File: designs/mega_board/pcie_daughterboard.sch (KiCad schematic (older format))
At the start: 13 parts

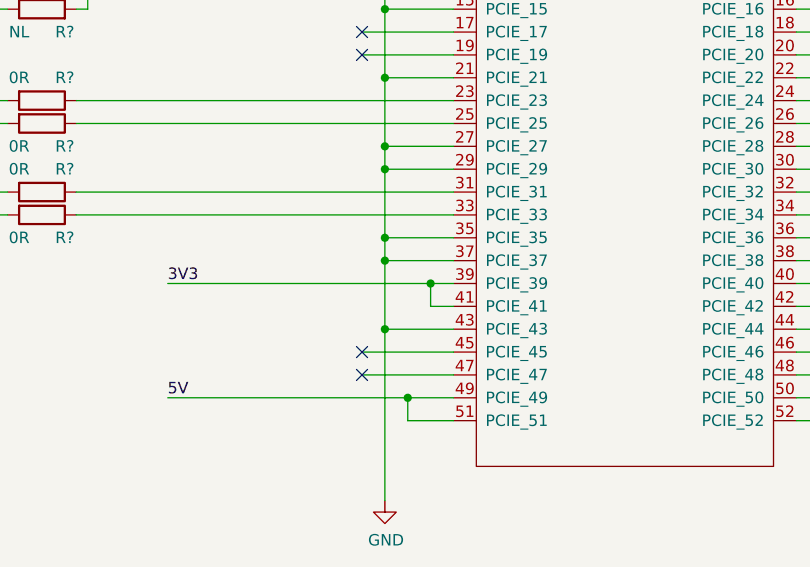
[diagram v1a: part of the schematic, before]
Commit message: Change PCIe pin 37 ground connection to not connected. Fixes #37
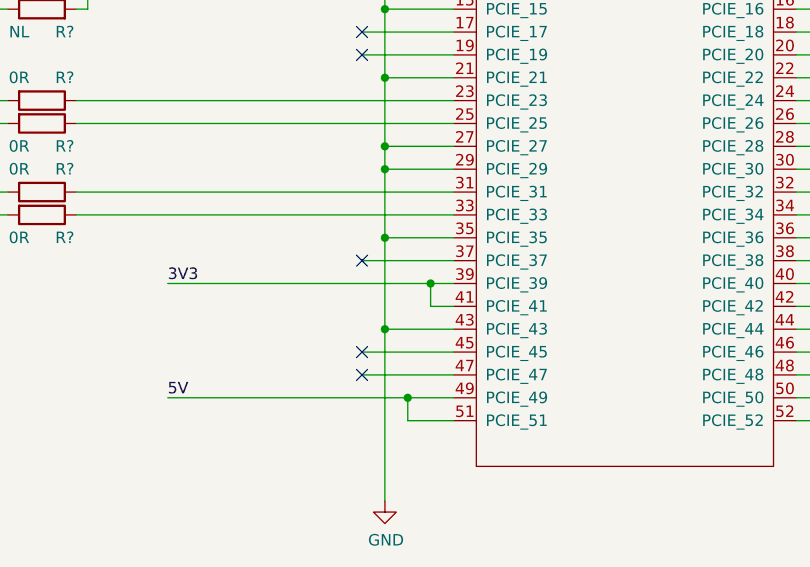
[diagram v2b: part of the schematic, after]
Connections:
- net GND: no longer U?.37 (PCIE_37)
- no-connect marks 13 -> 14
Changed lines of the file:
@@
 $Descr A4 11693 8268
 encoding utf-8
-Sheet 8 14
+Sheet 11 14
 Title "LibreRouter - Megaboard"
 Date "2019-06-26"
@@
 	4650 4400 4650 4700
 Connection ~ 4650 4700
-Wire Wire Line
-	4650 4700 4650 4800
 Connection ~ 4650 5100
 Wire Wire Line
@@
 Wire Wire Line
 	3000 4600 2500 4600
-Connection ~ 4650 4800
-Wire Wire Line
-	4650 4800 4650 5100
 NoConn ~ 4550 3800
 NoConn ~ 4550 3900
@@
 	4650 5100 4950 5100
 Wire Wire Line
-	4650 4800 4950 4800
-Wire Wire Line
 	4650 4700 4950 4700
 Wire Wire Line
@@
 Wire Wire Line
 	6450 5100 7400 5100
+Wire Wire Line
+	4650 4700 4650 5100
+NoConn ~ 4550 4800
+Wire Wire Line
+	4550 4800 4950 4800
 $EndSCHEMATC

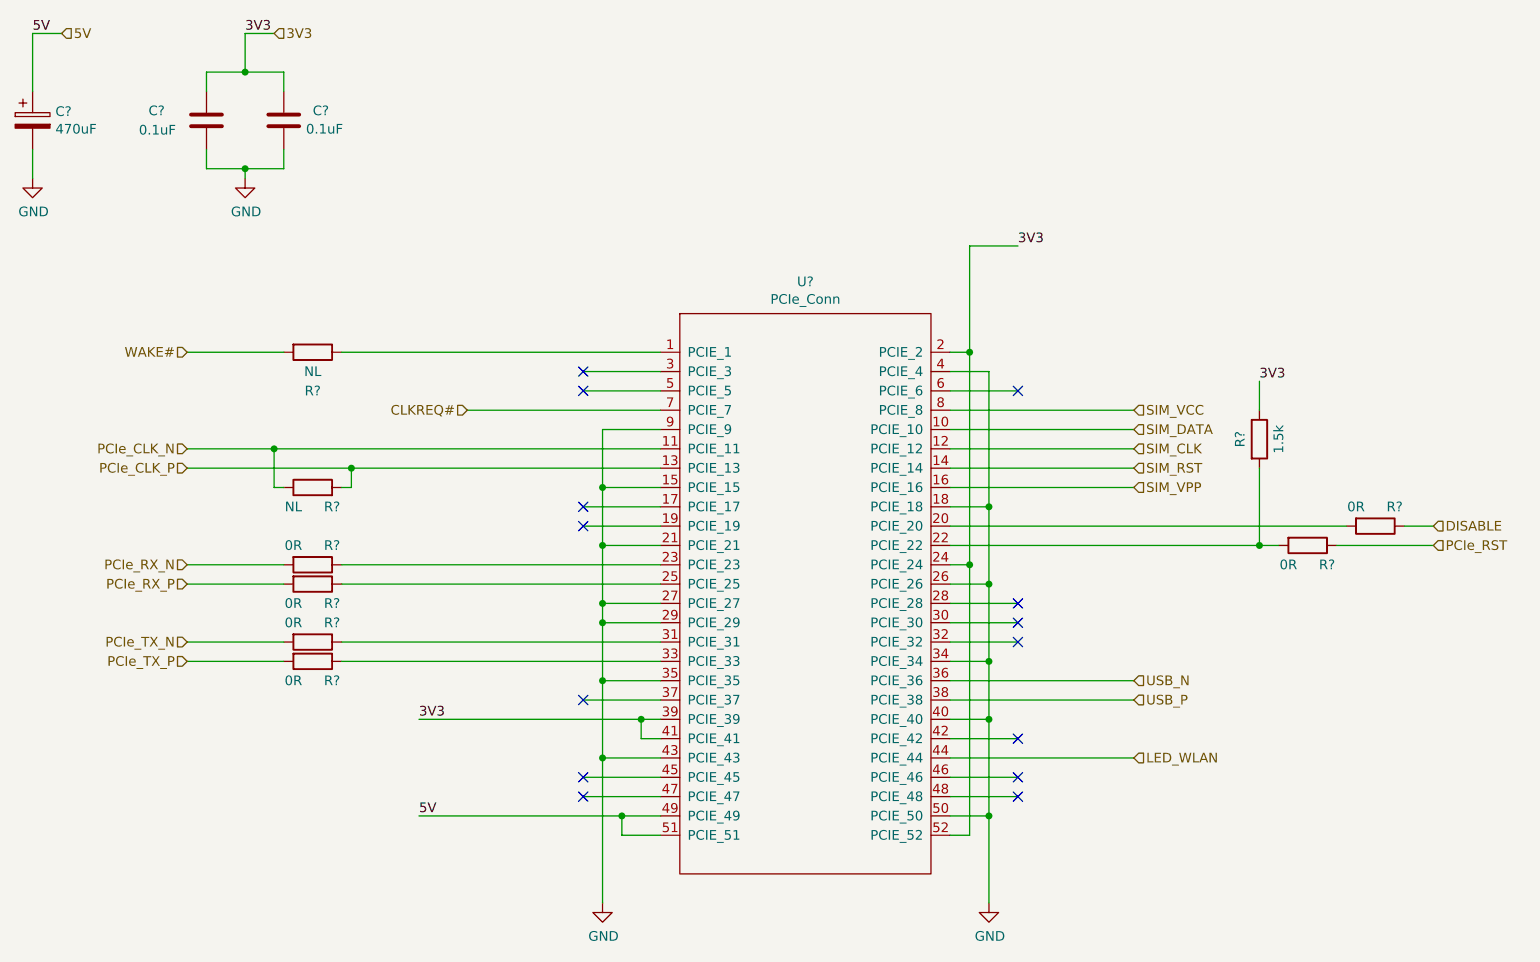
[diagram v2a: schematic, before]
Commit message: Enumerate components as is in eagle design.
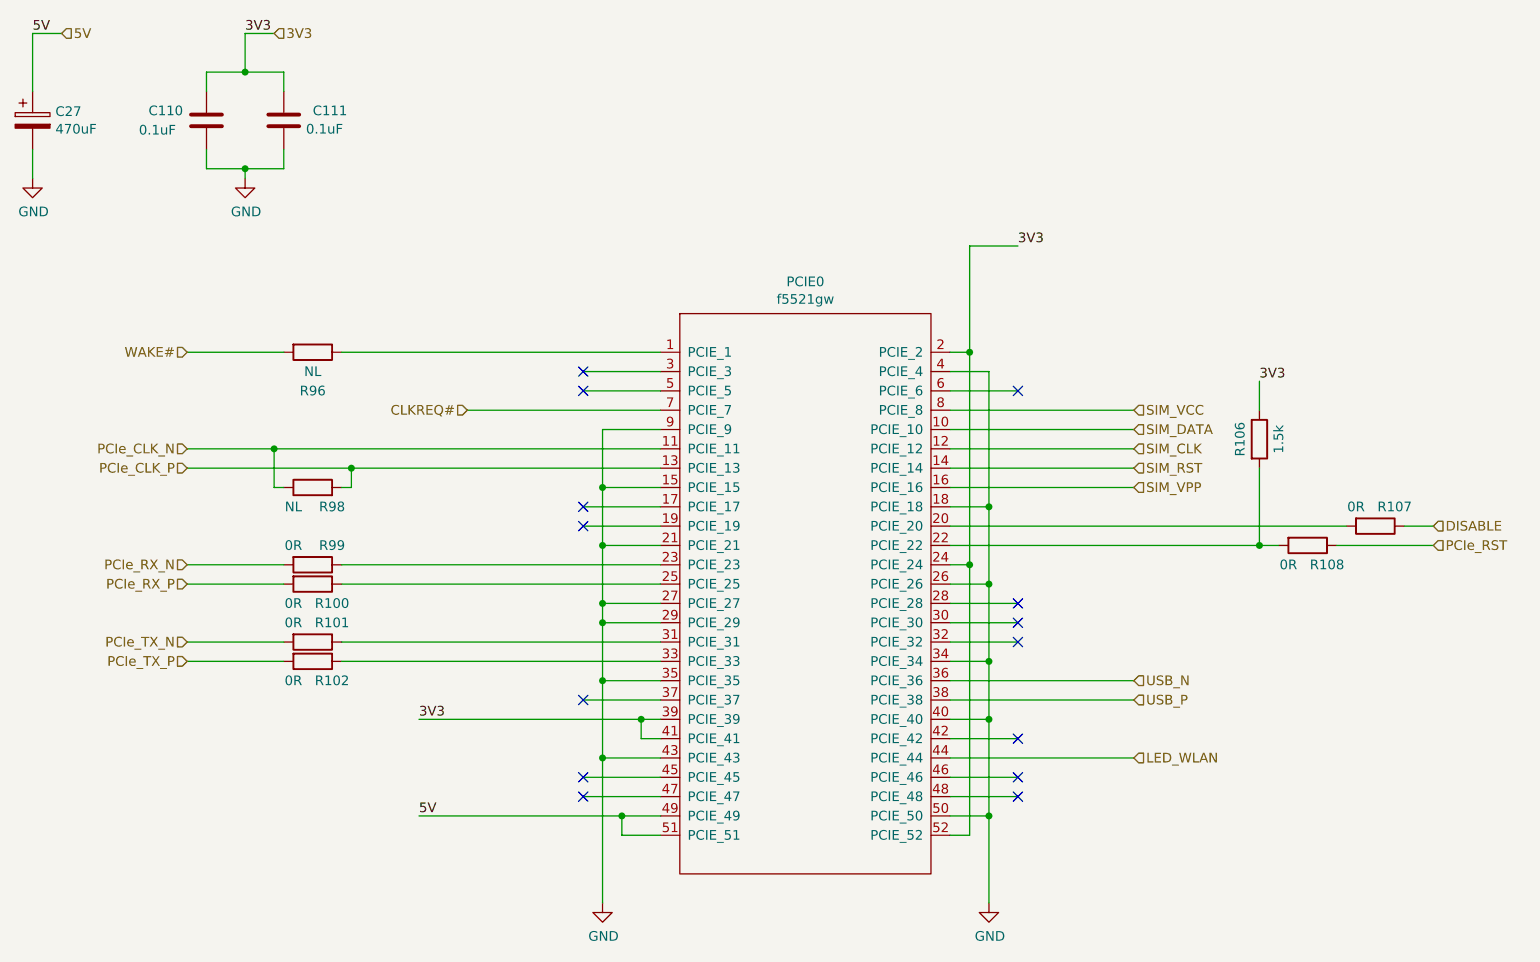
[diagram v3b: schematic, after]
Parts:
- C110, C111: renamed from C?; footprint (none) -> LibreRouter_MegaBoard:C0402
- C27: renamed from C?; footprint (none) -> LibreRouter_MegaBoard:UD-6,3X7,7_NICHICON
- PCIE0: renamed from U?; value PCIe_Conn -> f5521gw; footprint (none) -> LibreRouter_MegaBoard:MINI-PCI-E-FULL
- R100, R101, R102, R106, R107, R108, R96, R98, R99: renamed from R?; footprint (none) -> LibreRouter_MegaBoard:R0402
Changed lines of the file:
@@
 SIM_DATA
 $Comp
-L PCIe_Conn:PCIe_Conn U?
+L PCIe_Conn:PCIe_Conn PCIE0
 U 1 1 5D19C7E9
 P 5700 4250
-AR Path="/5D032C97/5D19C7E9" Ref="U?"  Part="1"
-AR Path="/5D1650F5/5D19C7E9" Ref="U?"  Part="1"
+AR Path="/5D032C97/5D19C7E9" Ref="PCIE0"  Part="1"
+AR Path="/5D1650F5/5D19C7E9" Ref="PCIE1"  Part="1"
 AR Path="/5D19C7E9" Ref="U?"  Part="1"
-F 0 "U?" H 5700 5865 50  0000 C CNN
-F 1 "PCIe_Conn" H 5700 5774 50  0000 C CNN
-F 2 "" H 5700 4250 50  0001 C CNN
+F 0 "PCIE0" H 5700 5865 50  0000 C CNN
+F 1 "f5521gw" H 5700 5774 50  0000 C CNN
+F 2 "LibreRouter_MegaBoard:MINI-PCI-E-FULL" H 5700 4250 50  0001 C CNN
 F 3 "" H 5700 4250 50  0001 C CNN
 	1    5700 4250
@@
 NoConn ~ 6800 5300
 $Comp
-L power:GND #PWR?
+L power:GND #PWR0173
 U 1 1 5D19F8AF
 P 6650 5850
-AR Path="/5D032C97/5D19F8AF" Ref="#PWR?"  Part="1"
-AR Path="/5D1650F5/5D19F8AF" Ref="#PWR?"  Part="1"
-F 0 "#PWR?" H 6650 5600 50  0001 C CNN
+AR Path="/5D032C97/5D19F8AF" Ref="#PWR0173"  Part="1"
+AR Path="/5D1650F5/5D19F8AF" Ref="#PWR0190"  Part="1"
+F 0 "#PWR0190" H 6650 5600 50  0001 C CNN
 F 1 "GND" H 6655 5677 50  0000 C CNN
 F 2 "" H 6650 5850 50  0001 C CNN
@@
 	6550 4100 6550 3000
 $Comp
-L Device:R R?
+L Device:R R108
 U 1 1 5D1A0459
 P 8300 4000
-AR Path="/5D032C97/5D1A0459" Ref="R?"  Part="1"
-AR Path="/5D1650F5/5D1A0459" Ref="R?"  Part="1"
-F 0 "R?" V 8400 4100 50  0000 C CNN
+AR Path="/5D032C97/5D1A0459" Ref="R108"  Part="1"
+AR Path="/5D1650F5/5D1A0459" Ref="R118"  Part="1"
+F 0 "R108" V 8400 4100 50  0000 C CNN
 F 1 "0R" V 8400 3900 50  0000 C CNN
-F 2 "" V 8230 4000 50  0001 C CNN
+F 2 "LibreRouter_MegaBoard:R0402" V 8230 4000 50  0001 C CNN
 F 3 "~" H 8300 4000 50  0001 C CNN
 	1    8300 4000
@@
 $EndComp
 $Comp
-L Device:R R?
+L Device:R R107
 U 1 1 5D1A04F3
 P 8650 3900
-AR Path="/5D032C97/5D1A04F3" Ref="R?"  Part="1"
-AR Path="/5D1650F5/5D1A04F3" Ref="R?"  Part="1"
-F 0 "R?" V 8550 4000 50  0000 C CNN
+AR Path="/5D032C97/5D1A04F3" Ref="R107"  Part="1"
+AR Path="/5D1650F5/5D1A04F3" Ref="R117"  Part="1"
+F 0 "R107" V 8550 4000 50  0000 C CNN
 F 1 "0R" V 8550 3800 50  0000 C CNN
-F 2 "" V 8580 3900 50  0001 C CNN
+F 2 "LibreRouter_MegaBoard:R0402" V 8580 3900 50  0001 C CNN
 F 3 "~" H 8650 3900 50  0001 C CNN
 	1    8650 3900
@@
 $EndComp
 $Comp
-L Device:R R?
+L Device:R R106
 U 1 1 5D1A051B
 P 8050 3450
-AR Path="/5D032C97/5D1A051B" Ref="R?"  Part="1"
-AR Path="/5D1650F5/5D1A051B" Ref="R?"  Part="1"
-F 0 "R?" V 7950 3450 50  0000 C CNN
+AR Path="/5D032C97/5D1A051B" Ref="R106"  Part="1"
+AR Path="/5D1650F5/5D1A051B" Ref="R116"  Part="1"
+F 0 "R106" V 7950 3450 50  0000 C CNN
 F 1 "1.5k" V 8150 3450 50  0000 C CNN
-F 2 "" V 7980 3450 50  0001 C CNN
+F 2 "LibreRouter_MegaBoard:R0402" V 7980 3450 50  0001 C CNN
 F 3 "~" H 8050 3450 50  0001 C CNN
 	1    8050 3450
@@
 	8800 3900 8950 3900
 $Comp
-L Device:R R?
+L Device:R R96
 U 1 1 5D1A5891
 P 3150 3000
-AR Path="/5D032C97/5D1A5891" Ref="R?"  Part="1"
-AR Path="/5D1650F5/5D1A5891" Ref="R?"  Part="1"
-F 0 "R?" V 3350 3000 50  0000 C CNN
+AR Path="/5D032C97/5D1A5891" Ref="R96"  Part="1"
+AR Path="/5D1650F5/5D1A5891" Ref="R20"  Part="1"
+F 0 "R96" V 3350 3000 50  0000 C CNN
 F 1 "NL" V 3250 3000 50  0000 C CNN
-F 2 "" V 3080 3000 50  0001 C CNN
+F 2 "LibreRouter_MegaBoard:R0402" V 3080 3000 50  0001 C CNN
 F 3 "~" H 3150 3000 50  0001 C CNN
 	1    3150 3000
@@
 	2500 3600 3350 3600
 $Comp
-L Device:R R?
+L Device:R R98
 U 1 1 5D1AF5AD
 P 3150 3700
-AR Path="/5D032C97/5D1AF5AD" Ref="R?"  Part="1"
-AR Path="/5D1650F5/5D1AF5AD" Ref="R?"  Part="1"
-F 0 "R?" V 3050 3600 50  0000 C CNN
+AR Path="/5D032C97/5D1AF5AD" Ref="R98"  Part="1"
+AR Path="/5D1650F5/5D1AF5AD" Ref="R49"  Part="1"
+F 0 "R98" V 3050 3600 50  0000 C CNN
 F 1 "NL" V 3050 3800 50  0000 C CNN
-F 2 "" V 3080 3700 50  0001 C CNN
+F 2 "LibreRouter_MegaBoard:R0402" V 3080 3700 50  0001 C CNN
 F 3 "~" H 3150 3700 50  0001 C CNN
 	1    3150 3700
@@
 3V3
 $Comp
-L Device:C C?
+L Device:C C110
 U 1 1 5D1C5785
 P 2600 1800
-AR Path="/5D032C97/5D1C5785" Ref="C?"  Part="1"
-AR Path="/5D1650F5/5D1C5785" Ref="C?"  Part="1"
-F 0 "C?" H 2300 1850 50  0000 L CNN
+AR Path="/5D032C97/5D1C5785" Ref="C110"  Part="1"
+AR Path="/5D1650F5/5D1C5785" Ref="C75"  Part="1"
+F 0 "C110" H 2300 1850 50  0000 L CNN
 F 1 "0.1uF" H 2250 1750 50  0000 L CNN
-F 2 "" H 2638 1650 50  0001 C CNN
+F 2 "LibreRouter_MegaBoard:C0402" H 2638 1650 50  0001 C CNN
 F 3 "~" H 2600 1800 50  0001 C CNN
 	1    2600 1800
@@
 $EndComp
 $Comp
-L Device:C C?
+L Device:C C111
 U 1 1 5D1C583F
 P 3000 1800
-AR Path="/5D032C97/5D1C583F" Ref="C?"  Part="1"
-AR Path="/5D1650F5/5D1C583F" Ref="C?"  Part="1"
-F 0 "C?" H 3150 1850 50  0000 L CNN
+AR Path="/5D032C97/5D1C583F" Ref="C111"  Part="1"
+AR Path="/5D1650F5/5D1C583F" Ref="C116"  Part="1"
+F 0 "C111" H 3150 1850 50  0000 L CNN
 F 1 "0.1uF" H 3115 1755 50  0000 L CNN
-F 2 "" H 3038 1650 50  0001 C CNN
+F 2 "LibreRouter_MegaBoard:C0402" H 3038 1650 50  0001 C CNN
 F 3 "~" H 3000 1800 50  0001 C CNN
 	1    3000 1800
@@
 $EndComp
 $Comp
-L power:GND #PWR?
+L power:GND #PWR0174
 U 1 1 5D1C58DE
 P 2800 2100
-AR Path="/5D032C97/5D1C58DE" Ref="#PWR?"  Part="1"
-AR Path="/5D1650F5/5D1C58DE" Ref="#PWR?"  Part="1"
-F 0 "#PWR?" H 2800 1850 50  0001 C CNN
+AR Path="/5D032C97/5D1C58DE" Ref="#PWR0174"  Part="1"
+AR Path="/5D1650F5/5D1C58DE" Ref="#PWR0191"  Part="1"
+F 0 "#PWR0191" H 2800 1850 50  0001 C CNN
 F 1 "GND" H 2805 1927 50  0000 C CNN
 F 2 "" H 2800 2100 50  0001 C CNN
@@
 	2950 1350 2800 1350
 $Comp
-L power:GND #PWR?
+L power:GND #PWR0175
 U 1 1 5D1D537C
 P 1700 2100
-AR Path="/5D032C97/5D1D537C" Ref="#PWR?"  Part="1"
-AR Path="/5D1650F5/5D1D537C" Ref="#PWR?"  Part="1"
-F 0 "#PWR?" H 1700 1850 50  0001 C CNN
+AR Path="/5D032C97/5D1D537C" Ref="#PWR0175"  Part="1"
+AR Path="/5D1650F5/5D1D537C" Ref="#PWR0192"  Part="1"
+F 0 "#PWR0192" H 1700 1850 50  0001 C CNN
 F 1 "GND" H 1705 1927 50  0000 C CNN
 F 2 "" H 1700 2100 50  0001 C CNN
@@
 	1850 1350 1700 1350
 $Comp
-L Device:CP C?
+L Device:CP C27
 U 1 1 5D1D8CB3
 P 1700 1800
-AR Path="/5D032C97/5D1D8CB3" Ref="C?"  Part="1"
-AR Path="/5D1650F5/5D1D8CB3" Ref="C?"  Part="1"
-F 0 "C?" H 1818 1846 50  0000 L CNN
+AR Path="/5D032C97/5D1D8CB3" Ref="C27"  Part="1"
+AR Path="/5D1650F5/5D1D8CB3" Ref="C43"  Part="1"
+F 0 "C27" H 1818 1846 50  0000 L CNN
 F 1 "470uF" H 1818 1755 50  0000 L CNN
-F 2 "" H 1738 1650 50  0001 C CNN
+F 2 "LibreRouter_MegaBoard:UD-6,3X7,7_NICHICON" H 1738 1650 50  0001 C CNN
 F 3 "~" H 1700 1800 50  0001 C CNN
 	1    1700 1800
@@
 	2500 4100 3000 4100
 $Comp
-L Device:R R?
+L Device:R R99
 U 1 1 5D1F3D95
 P 3150 4100
-AR Path="/5D032C97/5D1F3D95" Ref="R?"  Part="1"
-AR Path="/5D1650F5/5D1F3D95" Ref="R?"  Part="1"
-F 0 "R?" V 3050 4200 50  0000 C CNN
+AR Path="/5D032C97/5D1F3D95" Ref="R99"  Part="1"
+AR Path="/5D1650F5/5D1F3D95" Ref="R80"  Part="1"
+F 0 "R99" V 3050 4200 50  0000 C CNN
 F 1 "0R" V 3050 4000 50  0000 C CNN
-F 2 "" V 3080 4100 50  0001 C CNN
+F 2 "LibreRouter_MegaBoard:R0402" V 3080 4100 50  0001 C CNN
 F 3 "~" H 3150 4100 50  0001 C CNN
 	1    3150 4100
@@
 $EndComp
 $Comp
-L Device:R R?
+L Device:R R100
 U 1 1 5D1F3F5D
 P 3150 4200
-AR Path="/5D032C97/5D1F3F5D" Ref="R?"  Part="1"
-AR Path="/5D1650F5/5D1F3F5D" Ref="R?"  Part="1"
-F 0 "R?" V 3250 4300 50  0000 C CNN
+AR Path="/5D032C97/5D1F3F5D" Ref="R100"  Part="1"
+AR Path="/5D1650F5/5D1F3F5D" Ref="R110"  Part="1"
+F 0 "R100" V 3250 4300 50  0000 C CNN
 F 1 "0R" V 3250 4100 50  0000 C CNN
-F 2 "" V 3080 4200 50  0001 C CNN
+F 2 "LibreRouter_MegaBoard:R0402" V 3080 4200 50  0001 C CNN
 F 3 "~" H 3150 4200 50  0001 C CNN
 	1    3150 4200
@@
 	2500 4500 3000 4500
 $Comp
-L Device:R R?
+L Device:R R101
 U 1 1 5D1F7584
 P 3150 4500
-AR Path="/5D032C97/5D1F7584" Ref="R?"  Part="1"
-AR Path="/5D1650F5/5D1F7584" Ref="R?"  Part="1"
-F 0 "R?" V 3050 4600 50  0000 C CNN
+AR Path="/5D032C97/5D1F7584" Ref="R101"  Part="1"
+AR Path="/5D1650F5/5D1F7584" Ref="R111"  Part="1"
+F 0 "R101" V 3050 4600 50  0000 C CNN
 F 1 "0R" V 3050 4400 50  0000 C CNN
-F 2 "" V 3080 4500 50  0001 C CNN
+F 2 "LibreRouter_MegaBoard:R0402" V 3080 4500 50  0001 C CNN
 F 3 "~" H 3150 4500 50  0001 C CNN
 	1    3150 4500
@@
 $EndComp
 $Comp
-L Device:R R?
+L Device:R R102
 U 1 1 5D1F758C
 P 3150 4600
-AR Path="/5D032C97/5D1F758C" Ref="R?"  Part="1"
-AR Path="/5D1650F5/5D1F758C" Ref="R?"  Part="1"
-F 0 "R?" V 3250 4700 50  0000 C CNN
+AR Path="/5D032C97/5D1F758C" Ref="R102"  Part="1"
+AR Path="/5D1650F5/5D1F758C" Ref="R112"  Part="1"
+F 0 "R102" V 3250 4700 50  0000 C CNN
 F 1 "0R" V 3250 4500 50  0000 C CNN
-F 2 "" V 3080 4600 50  0001 C CNN
+F 2 "LibreRouter_MegaBoard:R0402" V 3080 4600 50  0001 C CNN
 F 3 "~" H 3150 4600 50  0001 C CNN
 	1    3150 4600
@@
 NoConn ~ 4550 5300
 $Comp
-L power:GND #PWR?
+L power:GND #PWR0176
 U 1 1 5D20ABC1
 P 4650 5850
-AR Path="/5D032C97/5D20ABC1" Ref="#PWR?"  Part="1"
-AR Path="/5D1650F5/5D20ABC1" Ref="#PWR?"  Part="1"
-F 0 "#PWR?" H 4650 5600 50  0001 C CNN
+AR Path="/5D032C97/5D20ABC1" Ref="#PWR0176"  Part="1"
+AR Path="/5D1650F5/5D20ABC1" Ref="#PWR0193"  Part="1"
+F 0 "#PWR0193" H 4650 5600 50  0001 C CNN
 F 1 "GND" H 4655 5677 50  0000 C CNN
 F 2 "" H 4650 5850 50  0001 C CNN
